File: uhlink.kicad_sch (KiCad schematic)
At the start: 85 parts, among them J1 USB_C_Receptacle_USB2.0_16P, J10 TTL_CTRL, J11 TTL, J12 TTL_EXTRA, J13 BOOT0_SEL, J14 BOOT1_SEL, J15 MCU_DEBUG, J2 ARM_JTAG_SWD_20, J3 STDC14, J4 ARM_JTAG_SWD_10, J5 USB_C_Receptacle_USB2.0_16P, J6 USB_A, J7 VTTL_SEL, J8 PICO_3PIN_UART, J9 PICO_3PIN_SWD, U1 STM32F103CBTx, U2 XC6206PxxxMR, U3 USBLC6-2SC6, U4 CH334R, U5 CH9102F, U6 USBLC6-2SC6, U7 USBLC6-2SC6, Y1 8Mhz, Y2 12Mhz

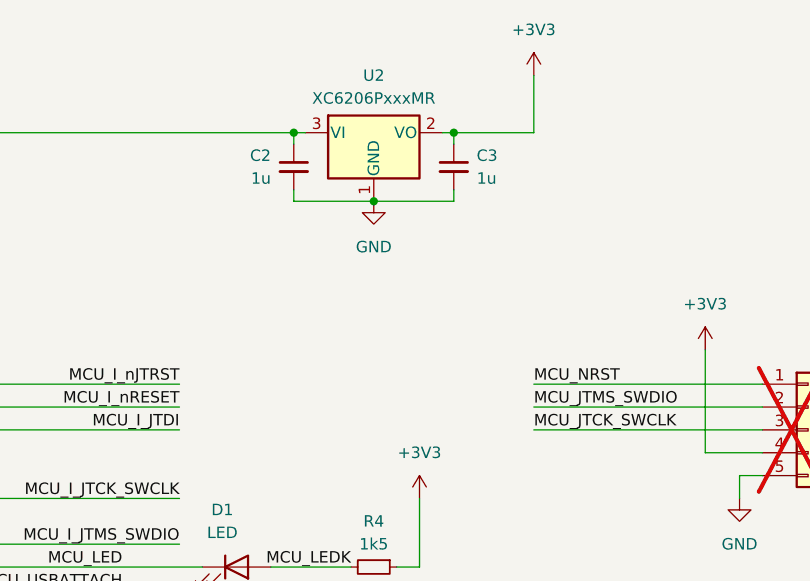
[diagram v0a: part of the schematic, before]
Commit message: feat: reannoate schematic, add pwr led
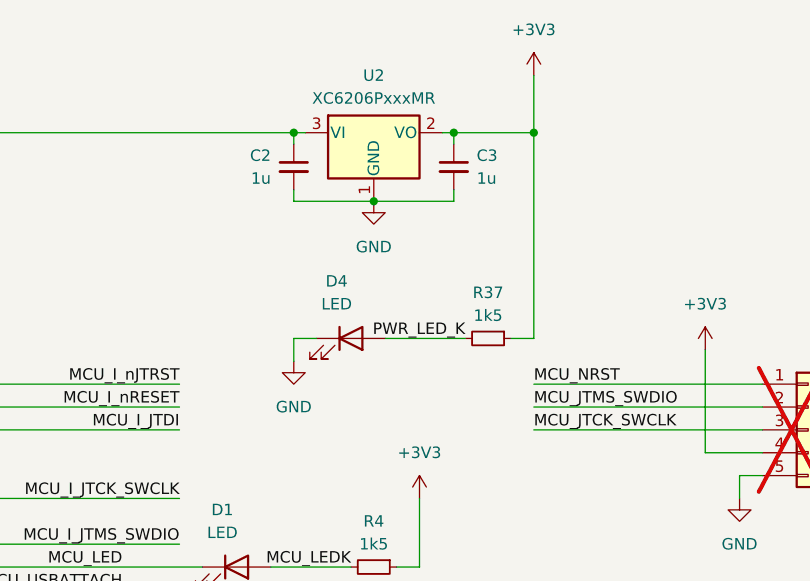
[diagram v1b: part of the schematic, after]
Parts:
- added D4: LED, symbol Device:LED
- added R37: 1k5, symbol Device:R_Small
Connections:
- net +3V3: now also R37.1
- net GND: now also D4.1 (K)
- new net PWR_LED_K: D4.2 (A), R37.2

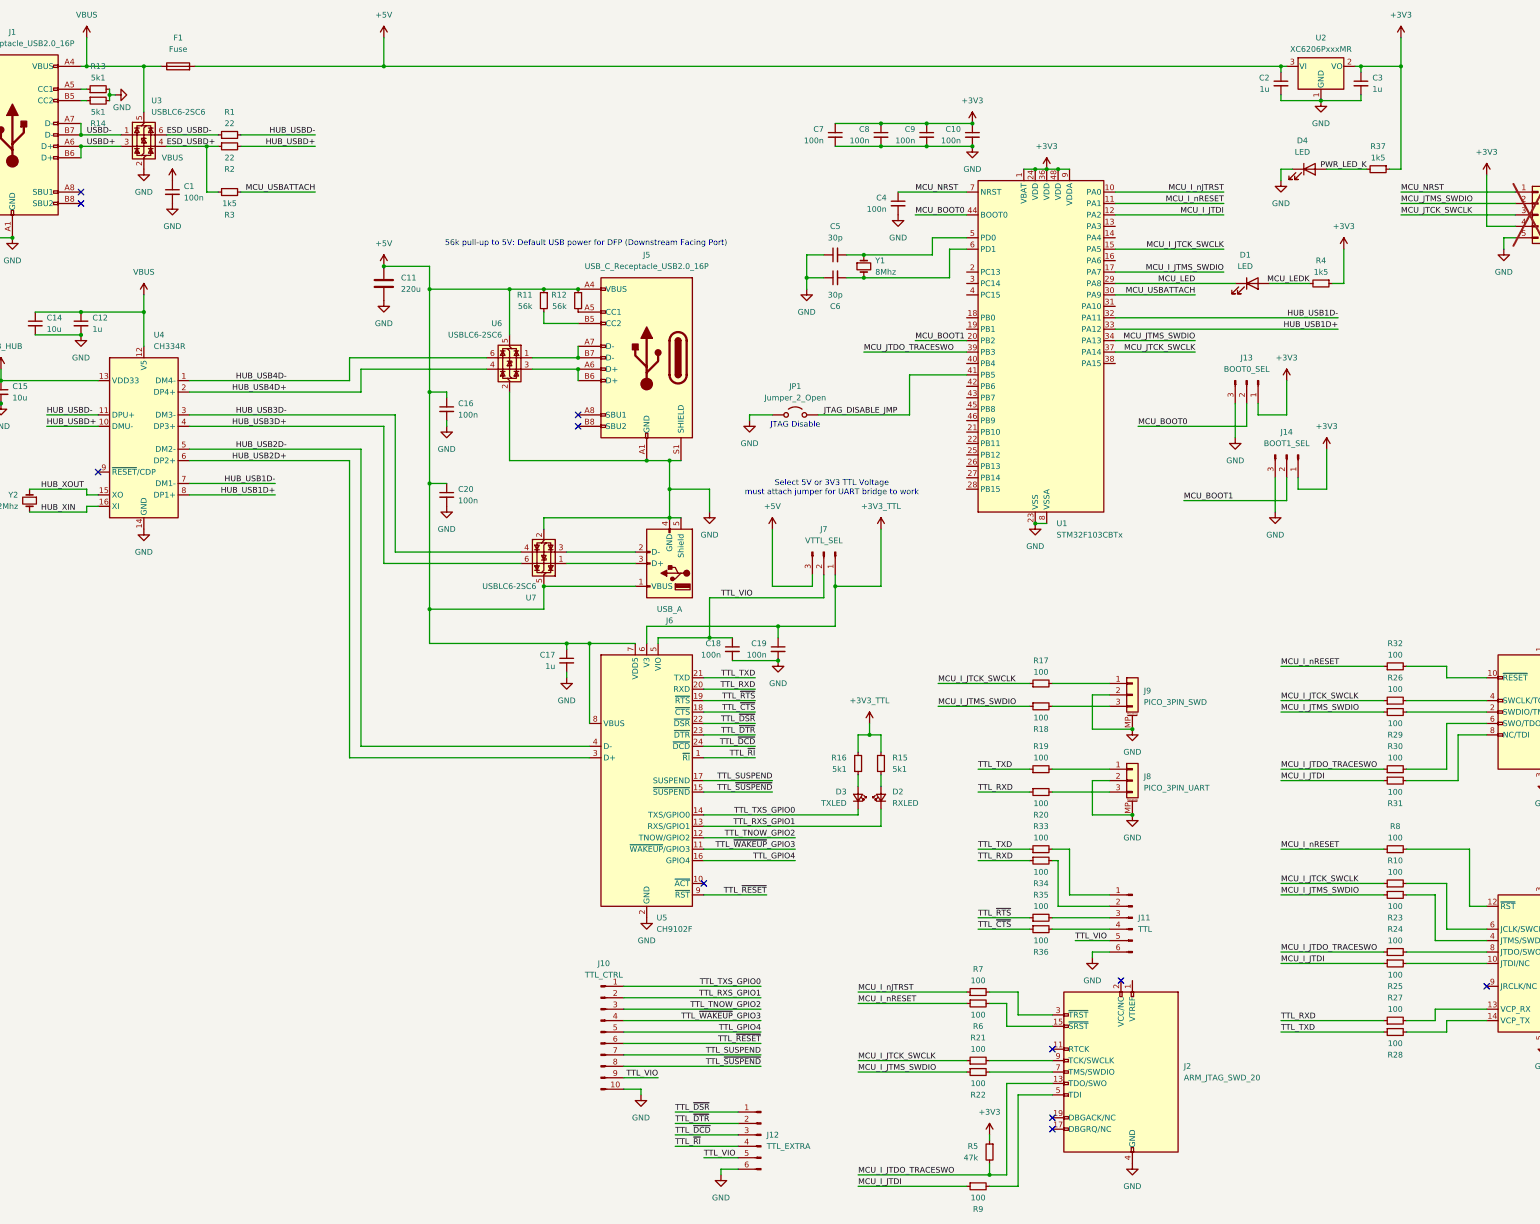
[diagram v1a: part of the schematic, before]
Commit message: feat: net classes+schematic colors, net labels
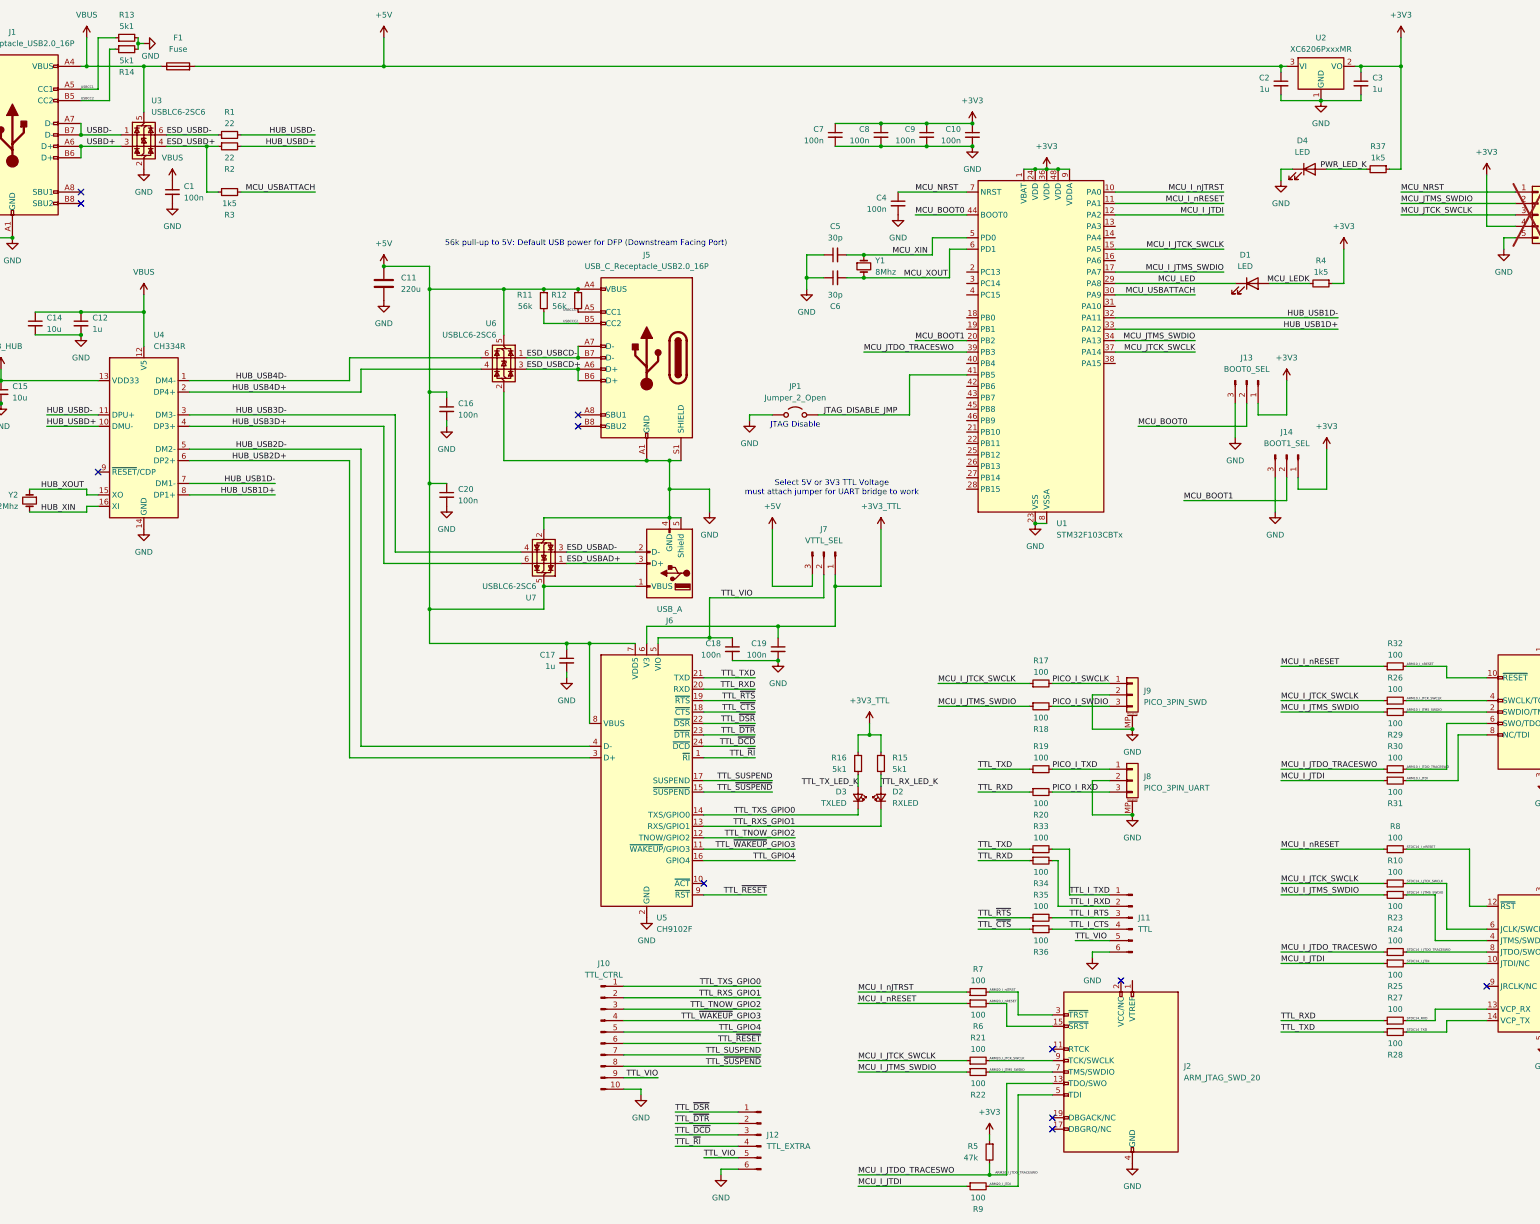
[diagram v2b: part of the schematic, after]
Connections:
- net USBCCC1: now reaches J5.A5 (CC1), R12.2
- net ESD_USBCD+: now reaches J5.A6 (D+), J5.B6 (D+), U6.3 (I/O2)
- net ESD_USBCD-: now reaches J5.A7 (D-), J5.B7 (D-), U6.1 (I/O1)
- net USBCCC2: now reaches J5.B5 (CC2), R11.2
- net TTL_TX_LED_K: now reaches D3.2 (A), R16.1
- net PICO_I_TXD: now reaches J8.1 (Pin_1), R19.2
- net PICO_I_RXD: now reaches J8.3 (Pin_3), R20.2
- net STDC14_I_JTDI: now reaches J3.10 (JTDI/NC), R25.2
- net STDC14_I_nRESET: now reaches J3.12 (~{RST}), R8.2
- net STDC14_RXD: now reaches J3.13 (VCP_RX), R27.2
- net STDC14_TXD: now reaches J3.14 (VCP_TX), R28.2
- net STDC14_I_JTMS_SWDIO: now reaches J3.4 (JTMS/SWDIO), R23.2
- net STDC14_I_JTCK_SWCLK: now reaches J3.6 (JCLK/SWCLK), R10.2
- net STDC14_I_JTDO_TRACESWO: now reaches J3.8 (JTDO/SWO), R24.2
- net MCU_XOUT: now reaches C6.2, U1.6 (PD1), Y1.2
- net USBCC1: now reaches J1.A5 (CC1), R13.1
- net USBCC2: now reaches J1.B5 (CC2), R14.1
- net ARM10_I_JTMS_SWDIO: now reaches J4.2 (SWDIO/TMS), R29.2
- net ARM20_I_JTMS_SWDIO: now reaches J2.7 (TMS/SWDIO), R22.2
- net ARM10_I_nRESET: now reaches J4.10 (~{RESET}), R32.2
- net TTL_I_CTS: now reaches J11.4 (Pin_4), R36.2
- net PICO_I_SWCLK: now reaches J9.1 (Pin_1), R17.2
- net PICO_I_SWDIO: now reaches J9.3 (Pin_3), R18.2
- net ESD_USBAD-: now reaches J6.2 (D-), U7.3 (I/O2)
- net ESD_USBAD+: now reaches J6.3 (D+), U7.1 (I/O1)
- net TTL_I_TXD: now reaches J11.1 (Pin_1), R33.2
- net TTL_I_RXD: now reaches J11.2 (Pin_2), R34.2
- net TTL_I_RTS: now reaches J11.3 (Pin_3), R35.2
- net ARM20_I_nJTRST: now reaches J2.3 (~{TRST}), R7.2
- net MCU_XIN: now reaches C5.2, U1.5 (PD0), Y1.1
- net ARM20_I_nRESET: now reaches J2.15 (~{SRST}), R6.2
- net ARM20_I_JTDI: now reaches J2.5 (TDI), R9.2
- net ARM20_I_JTCK_SWCLK: now reaches J2.9 (TCK/SWCLK), R21.2
- net ARM10_I_JTDO_TRACESWO: now reaches J4.6 (SWO/TDO), R30.2
- net ARM10_I_JTCK_SWCLK: now reaches J4.4 (SWCLK/TCK), R26.2
- net TTL_RX_LED_K: now reaches D2.2 (A), R15.1
- net ARM10_I_JTDI: now reaches J4.8 (NC/TDI), R31.2
- net MCU_I_JTDO_TRACESWO renamed ARM20_I_JTDO_TRACESWO
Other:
- moved on the sheet: R13, R14, U6

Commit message: feat: pre-layoutand adjustments
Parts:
- removed Y2: 12Mhz, symbol Device:Crystal_Small
- added Y2: 12MHz, Crystal:Crystal_SMD_3225-4Pin_3.2x2.5mm, symbol Device:Crystal_GND24_Small
- C1, C10, C13, C16, C18, C19, C20, C4, C7, C8, C9: footprint (none) -> Capacitor_SMD:C_0402_1005Metric; LCSC (none) -> C1525
- C11: footprint (none) -> Capacitor_THT:C_Radial_D10.0mm_H16.0mm_P5.00mm; LCSC (none) -> C2873996
- C12, C17, C2, C3: footprint (none) -> Capacitor_SMD:C_0402_1005Metric; LCSC (none) -> C52923
- C14, C15: footprint (none) -> Capacitor_SMD:C_0402_1005Metric; LCSC (none) -> C15525
- C5, C6: footprint (none) -> Capacitor_SMD:C_0402_1005Metric; LCSC (none) -> C1570
- D1: value LED -> PWRLED; footprint (none) -> LED_SMD:LED_0805_2012Metric; LCSC (none) -> C84256
- D2: footprint (none) -> LED_SMD:LED_0805_2012Metric; LCSC (none) -> C2296
- D3, D4: footprint (none) -> LED_SMD:LED_0805_2012Metric; LCSC (none) -> C2297
- J1, J5: LCSC (none) -> C2765186
- J10, J11, J12, J13, J14, J2, J3, J4, J7, J8, J9, JP1: now not fitted
- R1, R2: footprint (none) -> Resistor_SMD:R_0402_1005Metric; LCSC (none) -> C25092
- R10, R17, R18, R19, R20, R21, R22, R23, R24, R25, R26, R27, R28, R29, R30, R31, R32, R33, R34, R35, R36, R6, R7, R8, R9: footprint (none) -> Resistor_SMD:R_0402_1005Metric; LCSC (none) -> C25076
- R11, R12: footprint (none) -> Resistor_SMD:R_0603_1608Metric; LCSC (none) -> C23206
- R13, R14, R15, R16: footprint (none) -> Resistor_SMD:R_0402_1005Metric; LCSC (none) -> C25905
- R3, R37, R4: footprint (none) -> Resistor_SMD:R_0402_1005Metric; LCSC (none) -> C25867
- R5: footprint (none) -> Resistor_SMD:R_0402_1005Metric; LCSC (none) -> C25792
- U1: LCSC (none) -> C8304
- U2: LCSC (none) -> C5446
- U3, U6, U7: LCSC (none) -> C7519
- U4: LCSC (none) -> C4154405
- U5: LCSC (none) -> C2858418
- Y1: value 8Mhz -> 8MHz; footprint (none) -> Crystal:Crystal_SMD_HC49-SD; LCSC (none) -> C12674
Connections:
- net ESD_USBAD+: now also U7.3 (I/O2); no longer U7.1 (I/O1)
- net ESD_USBAD-: now also U7.1 (I/O1); no longer U7.3 (I/O2)
- net GND: now also Y2.2, Y2.4
- net HUB_USB3D+: now also U7.4 (I/O2); no longer U7.6 (I/O1)
- net HUB_USB3D-: now also U7.6 (I/O1); no longer U7.4 (I/O2)
- net HUB_XIN: now also Y2.3
- net HUB_XOUT: now also Y2.1
- net TTL_GPIO4: now also J10.2 (Pin_2); no longer J10.5 (Pin_5)
- net TTL_RXS_GPIO1: now also J10.5 (Pin_5); no longer J10.2 (Pin_2)
- net TTL_SUSPEND: now also J10.1 (Pin_1); no longer J10.7 (Pin_7)
- net TTL_TNOW_GPIO2: now also J10.6 (Pin_6); no longer J10.3 (Pin_3)
- net TTL_TXS_GPIO0: now also J10.4 (Pin_4); no longer J10.1 (Pin_1)
- net TTL_~{RESET}: now also J10.8 (Pin_8); no longer J10.6 (Pin_6)
- net TTL_~{SUSPEND}: now also J10.3 (Pin_3); no longer J10.8 (Pin_8)
- net TTL_~{WAKEUP}_GPIO3: now also J10.7 (Pin_7); no longer J10.4 (Pin_4)
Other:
- note added: "TODO: SWAP THE TWO EXPANSION USBS FOR LAYOUT"
- moved on the sheet: U7

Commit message: feat: basic layout
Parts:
- J8, J9: footprint Connector_JST:JST_SH_SM03B-SRSS-TB_1x03-1MP_P1.00mm_Horizontal -> Connector_JST:JST_SH_BM03B-SRSS-TB_1x03-1MP_P1.00mm_Vertical
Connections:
- net ARM20_I_JTDO_TRACESWO: now also U1.31 (PA10)
- net ESD_USBAD+: now also U6.3 (I/O2); no longer U7.3 (I/O2)
- net ESD_USBAD-: now also U6.1 (I/O1); no longer U7.1 (I/O1)
- net ESD_USBCD+: now also U7.3 (I/O2); no longer U6.3 (I/O2)
- net ESD_USBCD-: now also U7.1 (I/O1); no longer U6.1 (I/O1)
- net HUB_USB1D+: now also U5.3 (D+); no longer U1.33 (PA12)
- net HUB_USB1D-: now also U5.4 (D-); no longer U1.32 (PA11)
- net HUB_USB2D+: now also U7.4 (I/O2); no longer U5.3 (D+)
- net HUB_USB2D-: now also U7.6 (I/O1); no longer U5.4 (D-)
- net HUB_USB3D+: now also U6.4 (I/O2); no longer U7.4 (I/O2)
- net HUB_USB3D-: now also U6.6 (I/O1); no longer U7.6 (I/O1)
- net HUB_USB4D+: now also U1.33 (PA12); no longer U6.4 (I/O2)
- net HUB_USB4D-: now also U1.32 (PA11); no longer U6.6 (I/O1)
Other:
- note removed: "TODO: SWAP THE TWO EXPANSION USBS FOR LAYOUT"
- moved on the sheet: C11, C16, C20, J5, J6, R11, R12, U6, U7
